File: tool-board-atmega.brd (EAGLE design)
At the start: 144 x 104 mm, 104 parts, among them IC3 ATMEGA2560-16AU, IC4 ATMEGA8U2-MU, Q1 16MHz, X1 22-23-2041, X2 MICROUSB_VERTICAL, X3 22-23-2041, X4 22-23-2041, Y2 16MHz

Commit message: Made revisions of Jaden's review
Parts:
- removed RESET-EN: (no value), jumper:SJ
- moved C1 5.24 mm to (-63.5, -36.8)
- moved C7 4.09 mm to (-64.4, -32.3)
- moved RN1 2.09 mm to (-59.2, -36.1)
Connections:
- net RESET: no longer RESET-EN.1, RESET-EN.2
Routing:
- net GND: track 76.5 -> 87.4 mm, vias 35 -> 38
- net PB5: track 127.5 -> 137.5 mm, vias 5 -> 3
- net PB6: track 129.6 -> 136.6 mm
- net RESET: track 97.3 -> 90.4 mm
- net N$63: track 0.00 -> 4.19 mm, vias 0 -> 2
- net DTR: track 41.8 -> 38.8 mm, vias 4 -> 3
- net N$33: track 20.0 -> 17.3 mm, vias 0 -> 2
- net N$35: track 12.5 -> 14.6 mm, vias 0 -> 2
- net PB7: track 122.8 -> 123.8 mm
- net N$15: track 190.5 -> 189.5 mm
- net NHOME-1: track 91.9 -> 92.6 mm
- net N$32: track 14.4 -> 15.1 mm, vias 0 -> 2
- net PA5: track 97.2 -> 96.8 mm, vias 3 -> 1
- net PA6: track 98.8 -> 98.6 mm, vias 4 -> 2
- net N$20: track 12.6 -> 12.8 mm, vias 0 -> 2

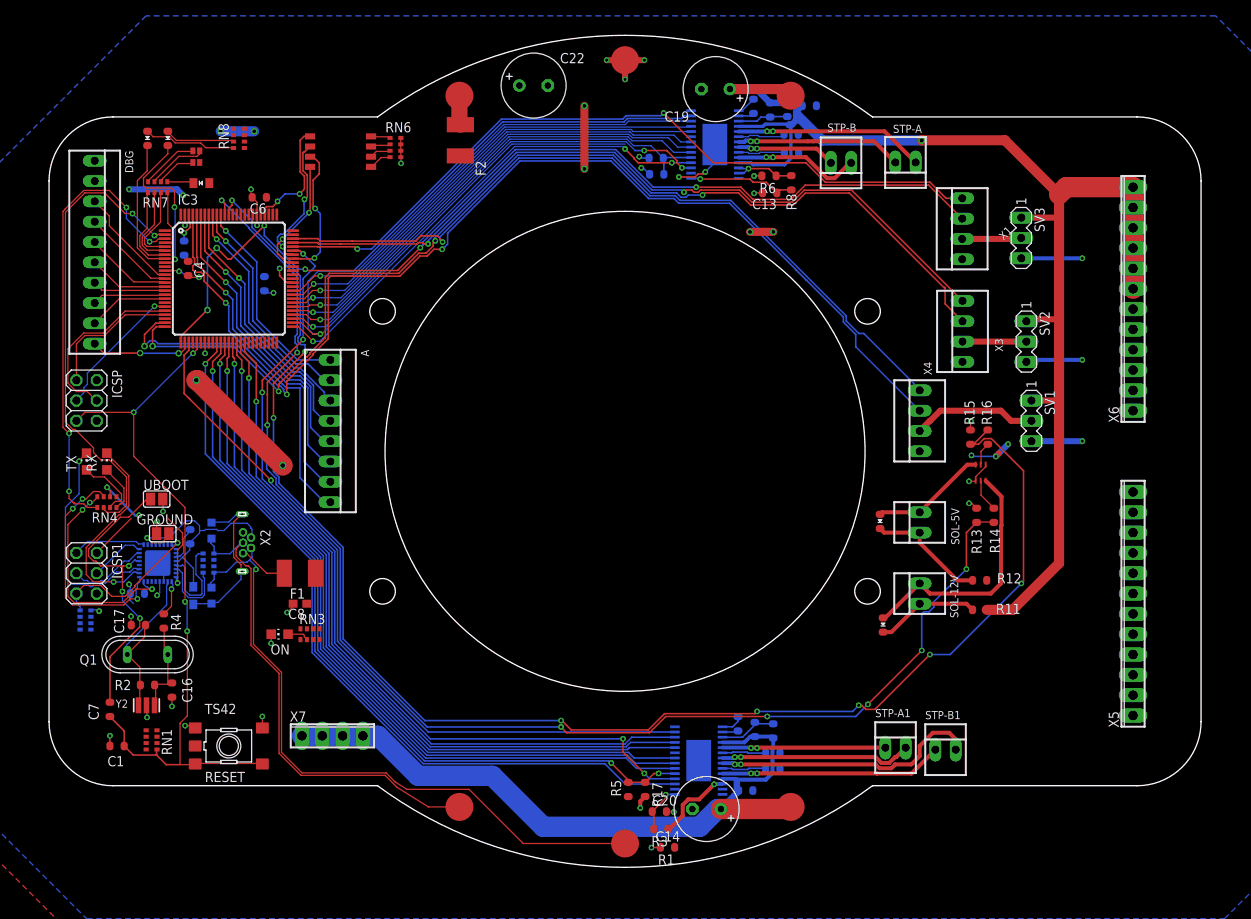
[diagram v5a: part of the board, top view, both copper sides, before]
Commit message: working on labeling fixes
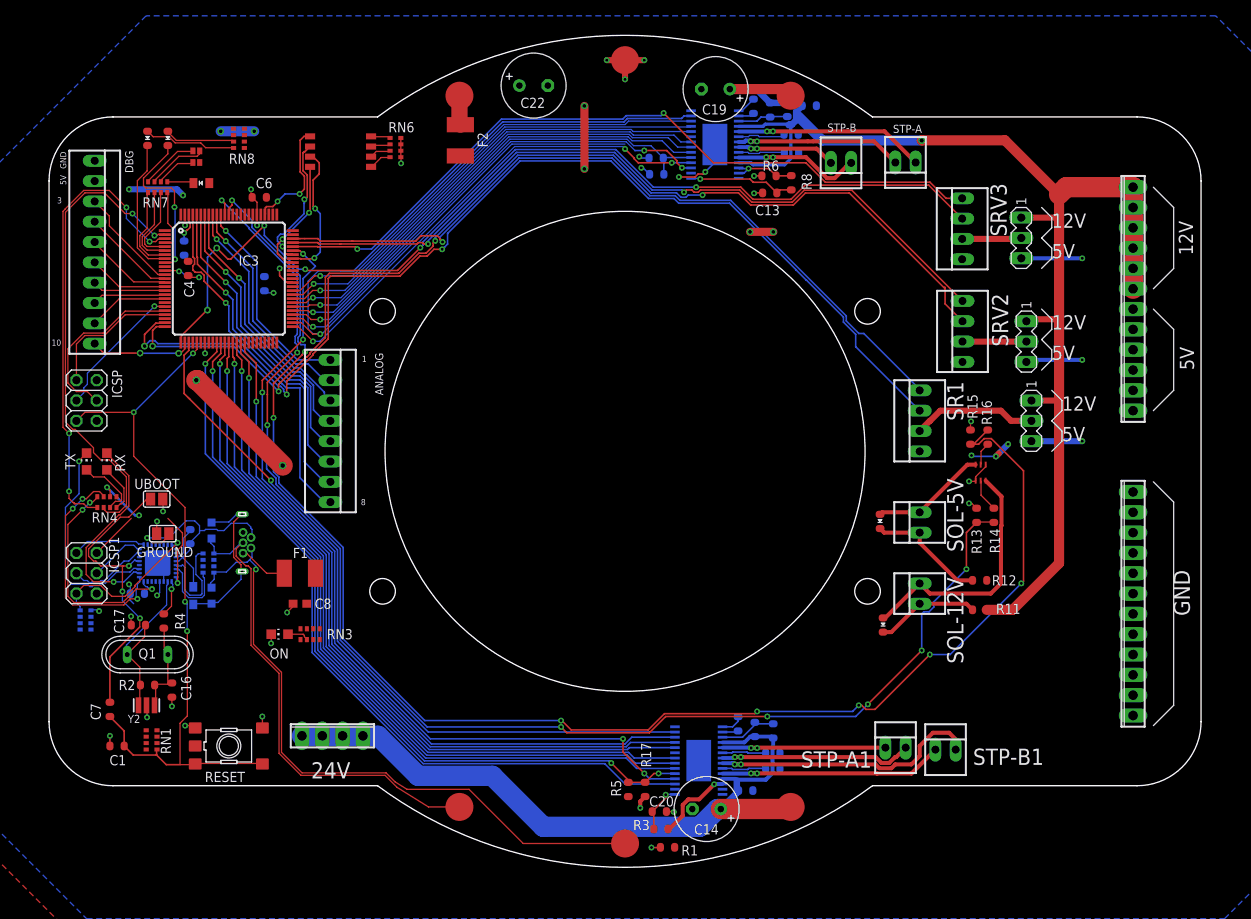
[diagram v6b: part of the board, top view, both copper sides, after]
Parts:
- renumbered A to ANALOG, U$1 to STP1, X1 to SRV3, X3 to SRV2, X4 to SR1, X5 to GND, X7 to 24V
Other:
- board text added: "1"
- board text added: "10"
- board text added: "12V"
- board text added: "3"
- board text added: "5V"
- board text added: "8"
- board text added: "GND"

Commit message: REV 1.0
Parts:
- removed ON: GREEN, led:CHIP-LED0805
- removed RN3: 1k, resistor-dil:CAY16
- removed U$7: DRV8825, ClinicalRobotics:DRV8825
- added 12, 24, 5: GREEN, led:CHIP-LED0805
- added R23: 1k, SmartPrj:R0603-ROUND
- added R24: 5k1, SmartPrj:R0603-ROUND
- added R25: 2k2, SmartPrj:R0603-ROUND
- added STP2: DRV8825, ClinicalRobotics:DRV8825
- moved STP1 77.0 mm to (9.21, -38.7)
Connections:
- removed net PA0: IC3.78
- removed net PA1: IC3.77
- removed net PA2: IC3.76
- removed net PA3: IC3.75
- removed net PA4: IC3.74
- removed net PB0: IC3.19
- removed net PB4: IC3.23
- removed net PD7: IC3.50
- removed net RXD3: IC3.63
- removed net TXD3: IC3.64
- removed net USBVCC: IC4.31
- new net N$64: 24.A, R24.2
- new net N$66: 12.A, R25.2
- net +12V: now also R25.1, STP2.11, STP2.4; no longer STP1.11, STP1.4
- net +24V: now also R24.1, STP1.11, STP1.4; no longer U$7.11, U$7.4
- net +5V: now also IC4.31, R23.1; no longer RN3.3
- net DECAY: now also STP2.19; no longer STP1.19
- net DECAY-1: now also STP1.19; no longer U$7.19
- net DIR: now also STP2.20; no longer STP1.20
- net DIR-1: now also STP1.20; no longer U$7.20
- net GND: now also 12.C, 24.C, 5.C, STP2.14, STP2.28, STP2.HEAT; no longer ON.C, U$7.14, U$7.28, U$7.HEAT
- net MODE0: now also STP2.24; no longer STP1.24
- net MODE0-1: now also STP1.24; no longer U$7.24
- net MODE1: now also STP2.25; no longer STP1.25
- net MODE1-1: now also STP1.25; no longer U$7.25
- net MODE2: now also STP2.26; no longer STP1.26
- net MODE2-1: now also STP1.26; no longer U$7.26
- net N$1: now also STP2.1; no longer STP1.1
- net N$12: now also STP2.8; no longer STP1.8
- net N$13: now also STP2.10; no longer STP1.10
- net N$14: now also STP2.15; no longer STP1.15
- net N$3: now also 5.A, R23.2; no longer ON.A, RN3.6
- net N$37: now also STP1.9; no longer U$7.9
- net N$39: now also STP1.1; no longer U$7.1
- net N$4: now also STP2.2; no longer STP1.2
- net N$40: now also STP1.2; no longer U$7.2
- net N$41: now also STP1.15; no longer U$7.15
- net N$42: now also STP1.12, STP1.13; no longer U$7.12, U$7.13
- net N$43: now also STP1.5; no longer U$7.5
- net N$44: now also STP1.7; no longer U$7.7
- net N$45: now also STP1.8; no longer U$7.8
- net N$46: now also STP1.10; no longer U$7.10
- net N$47: now also STP1.6; no longer U$7.6
- net N$48: now also STP2.6; no longer STP1.6
- net N$49: now also STP2.9; no longer STP1.9
- net N$6: now also STP2.12, STP2.13; no longer STP1.12, STP1.13
- net N$7: now also STP2.5; no longer STP1.5
- net N$8: now also STP2.7; no longer STP1.7
- net NENBL: now also STP2.21; no longer STP1.21
- net NENBL-1: now also STP1.21; no longer U$7.21
- net NFAULT: now also STP2.18; no longer STP1.18
- net NFAULT-1: now also STP1.18; no longer U$7.18
- net NHOME: now also STP2.27; no longer STP1.27
- net NHOME-1: now also STP1.27; no longer U$7.27
- net NRESET: now also STP2.16; no longer STP1.16
- net NRESET-1: now also STP1.16; no longer U$7.16
- net NSLEEP: now also STP2.17; no longer STP1.17
- net NSLEEP-1: now also STP1.17; no longer U$7.17
- net NSTEP: now also STP2.22; no longer STP1.22
- net NSTEP-1: now also STP1.22; no longer U$7.22
- net VCP: now also STP2.3; no longer STP1.3
- net VCP-1: now also STP1.3; no longer U$7.3
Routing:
- net NHOME: track 116.3 -> 68.6 mm
- net N$42: track 9.93 -> 14.1 mm
- net GND: track 87.4 -> 91.2 mm, vias 38 -> 40
- net +24V: track 90.0 -> 92.8 mm
- net +12V: track 169.3 -> 172.0 mm
- net N$64: track 0.00 -> 2.12 mm
- net N$66: track 0.00 -> 2.03 mm
- net N$38: track 5.01 -> 3.67 mm
- net +5V: track 64.9 -> 64.0 mm
- net DTR: track 38.8 -> 38.0 mm
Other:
- board text added: "Universal Tool Board Rev 1.0 Dylan Tomberlin For Cartesian Robotics"
